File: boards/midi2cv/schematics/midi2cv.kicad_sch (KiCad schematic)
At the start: 49 parts, among them J1 Jack-DC (12-32V), U1 LM7805_TO220, U2 6N138, U3 LM358, U4 MCP4822, U5 Pico, U6 LM358

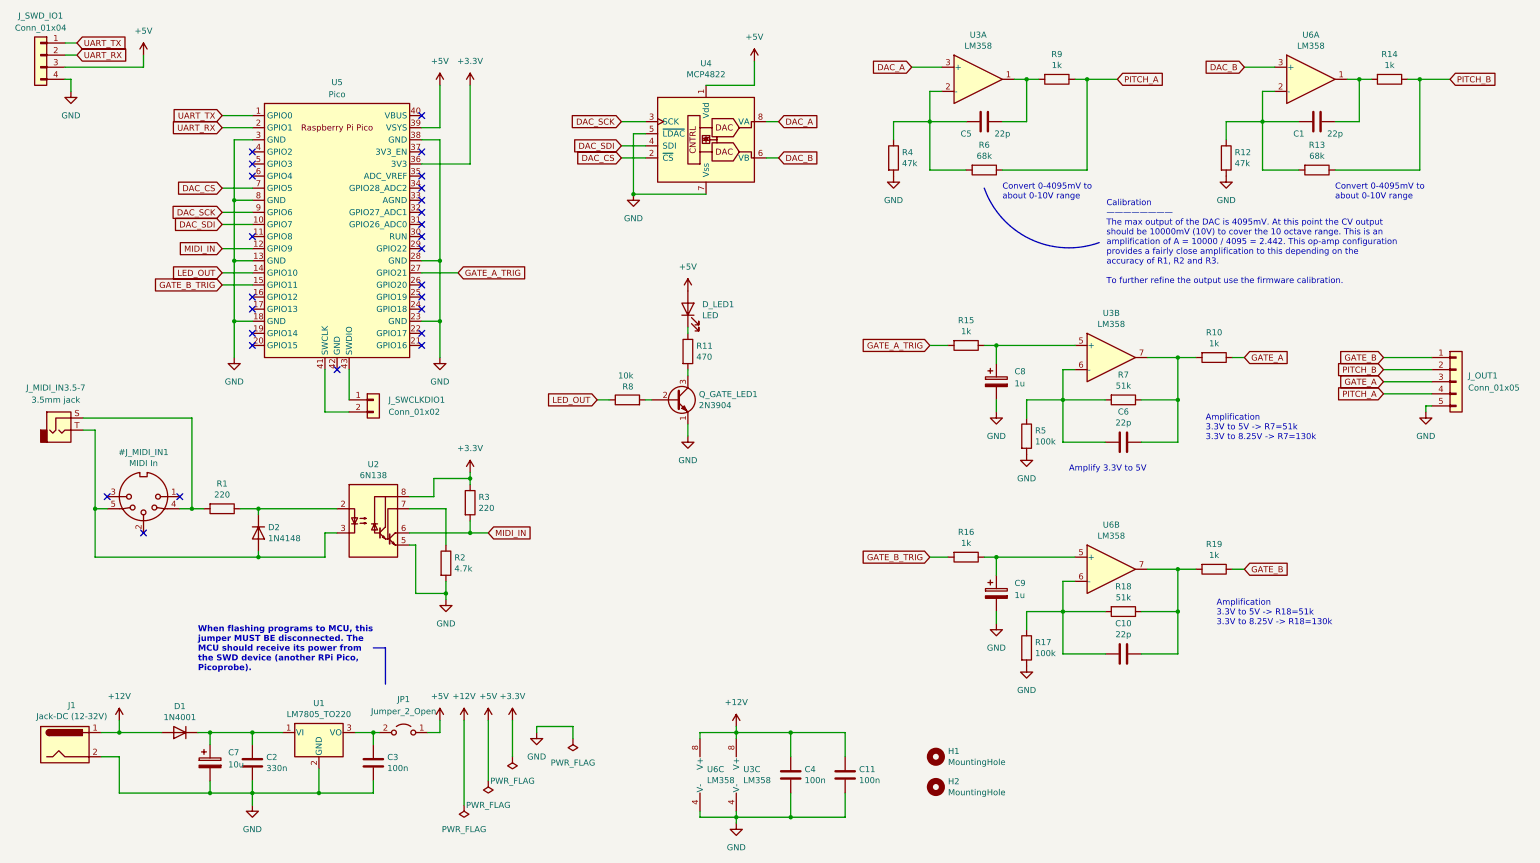
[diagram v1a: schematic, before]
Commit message: Replaced wired MIDI connection to pins
https://github.com/shmoergh/hog/issues/32

MIDI connection was done with manual wired NTS connectors. Now they are replaced with pins and pinheaders just like the other boards.
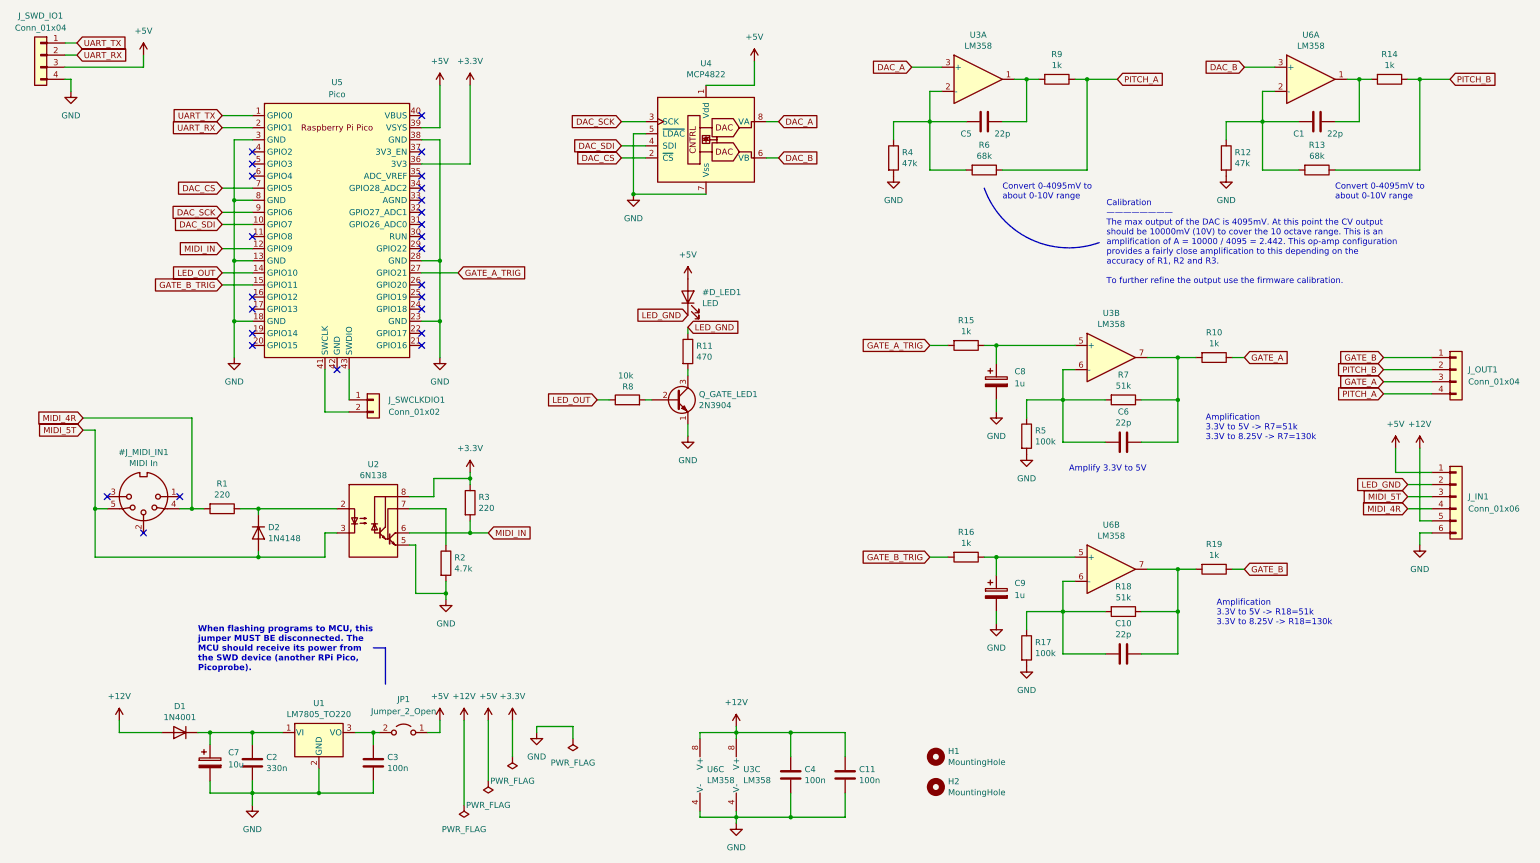
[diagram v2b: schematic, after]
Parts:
- removed J1: Jack-DC (12-32V), Shmoergh_Custom_Footprints:NSL25_01x02_Vertical, symbol Connector:Jack-DC
- removed J_MIDI_IN3.5-7: 3.5mm jack, Shmoergh_Custom_Footprints:NSL25_01x02_Vertical-AudioJack-TS, symbol Connector_Audio:AudioJack2
- removed J_OUT1: Conn_01x05, Shmoergh_Custom_Footprints:NSL25_01x05_Vertical, symbol Connector_Generic:Conn_01x05
- added J_IN1: Conn_01x06, Connector_PinHeader_2.54mm:PinHeader_1x06_P2.54mm_Vertical, symbol Connector_Generic:Conn_01x06
- added J_OUT1: Conn_01x04, Connector_PinHeader_2.54mm:PinHeader_1x04_P2.54mm_Vertical, symbol Connector_Generic:Conn_01x04
- renumbered D_LED1 to #D_LED1
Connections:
- net +12V: now also J_IN1.5 (Pin_5)
- net +5V: now also J_IN1.1 (Pin_1)
- net GATE_A: now also J_OUT1.3 (Pin_3)
- net GATE_B: now also J_OUT1.1 (Pin_1)
- net GND: now also J_IN1.6 (Pin_6)
- net PITCH_A: now also J_OUT1.4 (Pin_4)
- net PITCH_B: now also J_OUT1.2 (Pin_2)
- net LED_GND: now reaches #D_LED1.1 (K), R11.1
- net LED_GND: now also J_IN1.2 (Pin_2)
- net MIDI_4R: now reaches #J_MIDI_IN1.4, R1.2
- net MIDI_4R: now also J_IN1.4 (Pin_4)
- net MIDI_5T: now reaches #J_MIDI_IN1.5, D2.2 (A), U2.3 (C2)
- net MIDI_5T: now also J_IN1.3 (Pin_3)

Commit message: Added production files to MIDI2CV board
ref https://github.com/shmoergh/hog/issues/19
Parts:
- #D_LED1: now not fitted
- C1, C10, C5, C6: Part No. (none) -> 594-K220J15C0GF53L2; Part URL (none) -> https://mou.sr/3ZTXYXB; Vendor (none) -> Mouser
- C11, C3, C4: Part No. (none) -> 594-K103K15X7RF5TK2; Part URL (none) -> https://mou.sr/3VFZIRH; Vendor (none) -> Mouser
- C2: Part No. (none) -> 810-FA14X7R1H334KNU6; Part URL (none) -> https://mou.sr/4gDlMo9; Vendor (none) -> Mouser
- C7: Part No. (none) -> 80-ESS106M035AC2EA; Part URL (none) -> https://mou.sr/49DyMaU; Vendor (none) -> Mouser
- C8, C9: Part No. (none) -> 140-SG1R0M1H0407P; Part URL (none) -> https://mou.sr/41BqE8O; Vendor (none) -> Mouser
- D1: Part No. (none) -> 637-1N4001; Part URL (none) -> https://mou.sr/3DfEJyK; Vendor (none) -> Mouser
- D2: Part No. (none) -> 512-1N4148; Part URL (none) -> https://mou.sr/3ZP7Wt3; Vendor (none) -> Mouser
- JP1, J_SWCLKDIO1: Part No. (none) -> 737-PH1RB-02-UA; Part URL (none) -> https://mou.sr/3D93YT9; Vendor (none) -> Mouser
- J_IN1: Part No. (none) -> 737-RS1-06-G; Part URL (none) -> https://mou.sr/3BuZUME; Vendor (none) -> Mouser
- J_OUT1, J_SWD_IO1: Part No. (none) -> 737-RS1-04-G; Part URL (none) -> https://mou.sr/4gDjs0p; Vendor (none) -> Mouser
- Q_GATE_LED1: Part No. (none) -> 637-2N3904; Part URL (none) -> https://mou.sr/4febysZ; Vendor (none) -> Mouser
- R1, R3: Part No. (none) -> 303-MF0W4FF2200B00; Part URL (none) -> https://mou.sr/4iu83Sh; Vendor (none) -> Mouser
- R10, R14, R15, R16, R19, R9: Part No. (none) -> 303-MF0W4FF1001A10; Part URL (none) -> https://mou.sr/3De3mMa; Vendor (none) -> Mouser
- R11: Part No. (none) -> 303-MF0W4FF4700A10; Part URL (none) -> https://mou.sr/3DjrzRq; Vendor (none) -> Mouser
- R12, R4: Part No. (none) -> 303-CFR0W4J0473B00; Part URL (none) -> https://mou.sr/3VFb8Fd; Vendor (none) -> Mouser
- R13, R6: Part No. (none) -> 603-MFR-25FBF52-68K; Part URL (none) -> https://mou.sr/4gyTECt; Vendor (none) -> Mouser
- R17, R5: Part No. (none) -> 303-MF0W4FF1003T50; Part URL (none) -> https://mou.sr/3BGpE8K; Vendor (none) -> Mouser
- R18, R7: Part No. (none) -> 303-MF0W4FF5102B00; Part URL (none) -> https://mou.sr/3OXlwVc; Vendor (none) -> Mouser
- R2: Part No. (none) -> 303-MF0W4FF4701A10; Part URL (none) -> https://mou.sr/41yABnC; Vendor (none) -> Mouser
- R8: Part No. (none) -> 303-MF0W4FF1002T50; Part URL (none) -> https://mou.sr/4gfXSiu; Vendor (none) -> Mouser
- U1: Part No. (none) -> 926-LM7805CT/NOPB; Part URL (none) -> https://mou.sr/4gwivXu; Vendor (none) -> Mouser
- U2: Part No. (none) -> 859-6N138M; Part URL (none) -> https://mou.sr/3VDrRsD; Vendor (none) -> Mouser
- U3, U6: Part No. (none) -> 595-LM358P; Part URL (none) -> https://mou.sr/4izjQPc; Vendor (none) -> Mouser
- U4: Part No. (none) -> 579-MCP4822-E/P; Part URL (none) -> https://mou.sr/4gecDm5; Vendor (none) -> Mouser
- U5: Part No. (none) -> 358-SC0915; Part URL (none) -> https://mou.sr/49BoTdS; Vendor (none) -> Mouser
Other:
- note added: "This LED is on the UI board here it's just for illustration."

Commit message: Updated resistor Mouser no's and added full bom
- Some of the THT resistors in the BOM were referencing to products with min. 1000 pcs order quantity
- Added a full Mouser BOM which can be used to order all Mouser components by uploading to their BOM tool: https://hu.mouser.com/bom/
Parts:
- R1, R3: Part No. 303-MF0W4FF2200B00 -> 603-MFR-25FTF52-220R; Part URL https://mou.sr/4iu83Sh -> https://mou.sr/41wmEVF
- R10, R14, R15, R16, R19, R9: Part No. 303-MF0W4FF1001A10 -> 603-MFR-25FBF52-1K; Part URL https://mou.sr/3De3mMa -> https://mou.sr/43MmrAb
- R11: Part No. 303-MF0W4FF4700A10 -> 603-MFR-25FBF52-470R; Part URL https://mou.sr/3DjrzRq -> https://mou.sr/3XTF2Xk
- R12, R4: Part No. 303-CFR0W4J0473B00 -> 603-MFR-25FBF52-47K; Part URL https://mou.sr/3VFb8Fd -> https://mou.sr/3XWs8rz
- R13, R6: Part No. 603-MFR-25FBF52-68K -> 603-MFR-25FBF52-68K
- R17, R5: Part No. 303-MF0W4FF1003T50 -> 603-MFR-25FRF52100K; Part URL https://mou.sr/3BGpE8K -> https://mou.sr/4hEwI4G
- R18, R7: Part No. 303-MF0W4FF5102B00 -> 603-MFR-25FBF52-51K; Part URL https://mou.sr/3OXlwVc -> https://mou.sr/43NIOFo
- R2: Part No. 303-MF0W4FF4701A10 -> 603-MFR-25FBF52-4K7; Part URL https://mou.sr/41yABnC -> https://mou.sr/4i8N07f
- R8: Part No. 303-MF0W4FF1002T50 -> 603-MFR25SFRF52-10K; Part URL https://mou.sr/4gfXSiu -> https://mou.sr/3XU3MyE
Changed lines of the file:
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@@
 			)
 		)
-		(property "Part No." "303-MF0W4FF2200B00 "
+		(property "Part No." "603-MFR-25FTF52-220R"
 			(at 114.3 120.65 0)
 			(effects
@@
 			)
 		)
-		(property "Part URL" "https://mou.sr/4iu83Sh"
+		(property "Part URL" "https://mou.sr/41wmEVF"
 			(at 114.3 120.65 0)
 			(effects
@@
 			)
 		)
-		(property "Part No." "303-MF0W4FF1003T50 "
+		(property "Part No." "603-MFR-25FRF52100K"
 			(at 231.14 151.13 0)
 			(effects
@@
 			)
 		)
-		(property "Part URL" "https://mou.sr/3BGpE8K"
+		(property "Part URL" "https://mou.sr/4hEwI4G"
 			(at 231.14 151.13 0)
 			(effects
@@
 			)
 		)
-		(property "Part No." "303-CFR0W4J0473B00 "
+		(property "Part No." "603-MFR-25FBF52-47K"
 			(at 203.2 48.26 0)
 			(effects
@@
 			)
 		)
-		(property "Part URL" "https://mou.sr/3VFb8Fd"
+		(property "Part URL" "https://mou.sr/3XWs8rz"
 			(at 203.2 48.26 0)
 			(effects
@@
 			)
 		)
-		(property "Part No." "603-MFR-25FBF52-68K "
+		(property "Part No." "603-MFR-25FBF52-68K"
 			(at 292.1 50.8 0)
 			(effects
@@
 			)
 		)
-		(property "Part No." "303-MF0W4FF1001A10 "
+		(property "Part No." "603-MFR-25FBF52-1K"
 			(at 218.44 87.63 0)
 			(effects
@@
 			)
 		)
-		(property "Part URL" "https://mou.sr/3De3mMa"
+		(property "Part URL" "https://mou.sr/43MmrAb"
 			(at 218.44 87.63 0)
 			(effects
@@
 			)
 		)
-		(property "Part No." "303-MF0W4FF4701A10 "
+		(property "Part No." "603-MFR-25FBF52-4K7"
 			(at 109.22 133.35 0)
 			(effects
@@
 			)
 		)
-		(property "Part URL" "https://mou.sr/41yABnC"
+		(property "Part URL" "https://mou.sr/4i8N07f"
 			(at 109.22 133.35 0)
 			(effects
@@
 			)
 		)
-		(property "Part No." "303-MF0W4FF1001A10 "
+		(property "Part No." "603-MFR-25FBF52-1K"
 			(at 237.49 31.75 0)
 			(effects
@@
 			)
 		)
-		(property "Part URL" "https://mou.sr/3De3mMa"
+		(property "Part URL" "https://mou.sr/43MmrAb"
 			(at 237.49 31.75 0)
 			(effects
@@
 			)
 		)
-		(property "Part No." "603-MFR-25FBF52-68K "
+		(property "Part No." "603-MFR-25FBF52-68K"
 			(at 222.25 50.8 0)
 			(effects
@@
 			)
 		)
-		(property "Part No." "303-MF0W4FF5102B00 "
+		(property "Part No." "603-MFR-25FBF52-51K"
 			(at 251.46 99.06 0)
 			(effects
@@
 			)
 		)
-		(property "Part URL" "https://mou.sr/3OXlwVc"
+		(property "Part URL" "https://mou.sr/43NIOFo"
 			(at 251.46 99.06 0)
 			(effects
@@
 			)
 		)
-		(property "Part No." "303-CFR0W4J0473B00 "
+		(property "Part No." "603-MFR-25FBF52-47K"
 			(at 273.05 48.26 0)
 			(effects
@@
 			)
 		)
-		(property "Part URL" "https://mou.sr/3VFb8Fd"
+		(property "Part URL" "https://mou.sr/3XWs8rz"
 			(at 273.05 48.26 0)
 			(effects
@@
 			)
 		)
-		(property "Part No." "303-MF0W4FF1001A10 "
+		(property "Part No." "603-MFR-25FBF52-1K"
 			(at 270.51 90.17 0)
 			(effects
@@
 			)
 		)
-		(property "Part URL" "https://mou.sr/3De3mMa"
+		(property "Part URL" "https://mou.sr/43MmrAb"
 			(at 270.51 90.17 0)
 			(effects
@@
 			)
 		)
-		(property "Part No." "303-MF0W4FF5102B00 "
+		(property "Part No." "603-MFR-25FBF52-51K"
 			(at 251.46 143.51 0)
 			(effects
@@
 			)
 		)
-		(property "Part URL" "https://mou.sr/3OXlwVc"
+		(property "Part URL" "https://mou.sr/43NIOFo"
 			(at 251.46 143.51 0)
 			(effects
@@
 			)
 		)
-		(property "Part No." "303-MF0W4FF1001A10 "
+		(property "Part No." "603-MFR-25FBF52-1K"
 			(at 270.51 134.62 0)
 			(effects
@@
 			)
 		)
-		(property "Part URL" "https://mou.sr/3De3mMa"
+		(property "Part URL" "https://mou.sr/43MmrAb"
 			(at 270.51 134.62 0)
 			(effects
@@
 			)
 		)
-		(property "Part No." "303-MF0W4FF1001A10 "
+		(property "Part No." "603-MFR-25FBF52-1K"
 			(at 218.44 132.08 0)
 			(effects
@@
 			)
 		)
-		(property "Part URL" "https://mou.sr/3De3mMa"
+		(property "Part URL" "https://mou.sr/43MmrAb"
 			(at 218.44 132.08 0)
 			(effects
@@
 			)
 		)
-		(property "Part No." "303-MF0W4FF1001A10 "
+		(property "Part No." "603-MFR-25FBF52-1K"
 			(at 307.34 31.75 0)
 			(effects
@@
 			)
 		)
-		(property "Part URL" "https://mou.sr/3De3mMa"
+		(property "Part URL" "https://mou.sr/43MmrAb"
 			(at 307.34 31.75 0)
 			(effects
@@
 			)
 		)
-		(property "Part No." "303-MF0W4FF4700A10 "
+		(property "Part No." "603-MFR-25FBF52-470R"
 			(at 160.02 88.9 0)
 			(effects
@@
 			)
 		)
-		(property "Part URL" "https://mou.sr/3DjrzRq"
+		(property "Part URL" "https://mou.sr/3XTF2Xk"
 			(at 160.02 88.9 0)
 			(effects
@@
 			)
 		)
-		(property "Part No." "303-MF0W4FF1002T50 "
+		(property "Part No." "603-MFR25SFRF52-10K"
 			(at 147.32 99.06 0)
 			(effects
@@
 			)
 		)
-		(property "Part URL" "https://mou.sr/4gfXSiu"
+		(property "Part URL" "https://mou.sr/3XU3MyE"
 			(at 147.32 99.06 0)
 			(effects
@@
 			)
 		)
-		(property "Part No." "303-MF0W4FF1003T50 "
+		(property "Part No." "603-MFR-25FRF52100K"
 			(at 231.14 106.68 0)
 			(effects
@@
 			)
 		)
-		(property "Part URL" "https://mou.sr/3BGpE8K"
+		(property "Part URL" "https://mou.sr/4hEwI4G"
 			(at 231.14 106.68 0)
 			(effects
@@
 			)
 		)
-		(property "Part No." "303-MF0W4FF2200B00 "
+		(property "Part No." "603-MFR-25FTF52-220R"
 			(at 62.23 121.92 0)
 			(effects
@@
 			)
 		)
-		(property "Part URL" "https://mou.sr/4iu83Sh"
+		(property "Part URL" "https://mou.sr/41wmEVF"
 			(at 62.23 121.92 0)
 			(effects
